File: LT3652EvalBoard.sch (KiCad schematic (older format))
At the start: 40 parts, among them U1 LT3652

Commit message: Upload of Rev 0.5
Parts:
- removed Pload2: USB_A, ms_connectors:WURTH_ELEKTRONIK_629104151021, symbol USB_A
- added Wvin1: TEST_1P, ms_pcb_test_points:HARWIN_S1751-46, symbol TEST_1P
- Pbat1, Pload1: footprint w_conn_jst-ph:b2b-ph-kl -> w_conn_jst-ph:s2b-ph-kl
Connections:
- net at Dvin1.3 (A), Pslr1.1 (P1), Pslr2.1 (P1)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: now also Wvin1.1
- no-connect marks 4 -> 1
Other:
- moved on the sheet: Cbat1, Pload1
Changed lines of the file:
@@
 LIBS:valves
 LIBS:w_analog
+LIBS:ESP8266
 LIBS:LT3652EvalBoard-cache
 EELAYER 25 0
@@
 F 0 "Pbat1" H 7905 4160 50  0000 C CNN
 F 1 "JST PH" V 8005 4010 50  0000 C CNN
-F 2 "w_conn_jst-ph:b2b-ph-kl" H 7905 4010 50  0001 C CNN
+F 2 "w_conn_jst-ph:s2b-ph-kl" H 7905 4010 50  0001 C CNN
 F 3 "" H 7905 4010 50  0000 C CNN
 	1    7905 4010
@@
 L CONN_01X02 Pload1
 U 1 1 56CF675B
-P 8880 3200
-F 0 "Pload1" H 8880 3350 50  0000 C CNN
-F 1 "JST PH" V 8980 3200 50  0000 C CNN
-F 2 "w_conn_jst-ph:b2b-ph-kl" H 8880 3200 50  0001 C CNN
-F 3 "" H 8880 3200 50  0000 C CNN
-	1    8880 3200
-	1    0    0    -1
-$EndComp
-Wire Wire Line
-	8080 3150 8680 3150
+P 8790 2975
+F 0 "Pload1" H 8790 3125 50  0000 C CNN
+F 1 "JST PH" V 8890 2975 50  0000 C CNN
+F 2 "w_conn_jst-ph:s2b-ph-kl" H 8790 2975 50  0001 C CNN
+F 3 "" H 8790 2975 50  0000 C CNN
+	1    8790 2975
+	1    0    0    -1
+$EndComp
 $Comp
 L GND #PWR011
 U 1 1 56CF694F
-P 8630 3400
-F 0 "#PWR011" H 8630 3150 50  0001 C CNN
-F 1 "GND" H 8630 3250 50  0000 C CNN
-F 2 "" H 8630 3400 50  0000 C CNN
-F 3 "" H 8630 3400 50  0000 C CNN
-	1    8630 3400
-	1    0    0    -1
-$EndComp
-Wire Wire Line
-	8630 3250 8630 3400
-Wire Wire Line
-	8630 3250 8680 3250
+P 8540 3175
+F 0 "#PWR011" H 8540 2925 50  0001 C CNN
+F 1 "GND" H 8540 3025 50  0000 C CNN
+F 2 "" H 8540 3175 50  0000 C CNN
+F 3 "" H 8540 3175 50  0000 C CNN
+	1    8540 3175
+	1    0    0    -1
+$EndComp
+Wire Wire Line
+	8540 3025 8540 3175
+Wire Wire Line
+	8540 3025 8590 3025
 Text Notes 6450 3800 0    39   ~ 0
 4.2V FLT
@@
 L CP1_Small Cbat1
 U 1 1 56D1522A
-P 8370 3270
-F 0 "Cbat1" H 8380 3340 50  0000 L CNN
-F 1 "100uF" H 8380 3190 50  0000 L CNN
-F 2 "Capacitors_ThroughHole:C_Radial_D5_L6_P2.5" H 8370 3270 50  0001 C CNN
-F 3 "" H 8370 3270 50  0000 C CNN
-	1    8370 3270
-	1    0    0    -1
-$EndComp
-Wire Wire Line
-	8370 3370 8370 3385
-Wire Wire Line
-	8370 3385 8630 3385
-Connection ~ 8630 3385
-$Comp
-L USB_A Pload2
-U 1 1 56D16751
-P 8915 2640
-F 0 "Pload2" H 9115 2440 50  0000 C CNN
-F 1 "USB_A" H 8865 2840 50  0000 C CNN
-F 2 "ms_connectors:WURTH_ELEKTRONIK_629104151021" V 8865 2540 50  0001 C CNN
-F 3 "" V 8865 2540 50  0000 C CNN
-	1    8915 2640
-	0    1    1    0
-$EndComp
-$Comp
-L GND #PWR012
-U 1 1 56D16B0E
-P 8555 2865
-F 0 "#PWR012" H 8555 2615 50  0001 C CNN
-F 1 "GND" H 8555 2715 50  0000 C CNN
-F 2 "" H 8555 2865 50  0000 C CNN
-F 3 "" H 8555 2865 50  0000 C CNN
-	1    8555 2865
-	1    0    0    -1
-$EndComp
-Wire Wire Line
-	8555 2865 8555 2740
-Wire Wire Line
-	8555 2740 8615 2740
-NoConn ~ 8615 2540
-NoConn ~ 8615 2640
-NoConn ~ 9015 2940
-Wire Wire Line
-	8370 3170 8370 3150
-Connection ~ 8370 3150
-Wire Wire Line
-	8080 2440 8615 2440
+P 8280 3045
+F 0 "Cbat1" H 8290 3115 50  0000 L CNN
+F 1 "100uF" H 8290 2965 50  0000 L CNN
+F 2 "Capacitors_ThroughHole:C_Radial_D5_L6_P2.5" H 8280 3045 50  0001 C CNN
+F 3 "" H 8280 3045 50  0000 C CNN
+	1    8280 3045
+	1    0    0    -1
+$EndComp
+Wire Wire Line
+	8280 3145 8280 3160
+Wire Wire Line
+	8280 3160 8540 3160
+Connection ~ 8540 3160
+Wire Wire Line
+	8280 2850 8280 2945
+Connection ~ 8280 2925
 $Comp
 L CONN_01X02 Pslr1
@@
 $EndComp
 Wire Wire Line
-	7980 2925 8080 2925
-Connection ~ 8080 2925
-Wire Wire Line
 	7360 3175 7360 3960
 Wire Wire Line
@@
 Connection ~ 7625 2675
 $Comp
-L PWR_FLAG #FLG013
+L PWR_FLAG #FLG012
 U 1 1 56D7B958
-P 8315 2400
-F 0 "#FLG013" H 8315 2495 50  0001 C CNN
-F 1 "PWR_FLAG" H 8315 2580 50  0000 C CNN
-F 2 "" H 8315 2400 50  0000 C CNN
-F 3 "" H 8315 2400 50  0000 C CNN
-	1    8315 2400
-	1    0    0    -1
-$EndComp
-Wire Wire Line
-	8315 2400 8315 2440
-Connection ~ 8315 2440
+P 8280 2850
+F 0 "#FLG012" H 8280 2945 50  0001 C CNN
+F 1 "PWR_FLAG" H 8280 3030 50  0000 C CNN
+F 2 "" H 8280 2850 50  0000 C CNN
+F 3 "" H 8280 2850 50  0000 C CNN
+	1    8280 2850
+	1    0    0    -1
+$EndComp
 $Comp
 L CONN_01X02 Pslr2
@@
 	3950 3805 3915 3805
 Wire Wire Line
-	8080 2440 8080 3150
-Wire Wire Line
 	7360 3960 7705 3960
+Wire Wire Line
+	8590 2925 7980 2925
+$Comp
+L TEST_1P Wvin1
+U 1 1 56F07523
+P 4670 1810
+F 0 "Wvin1" H 4670 2005 50  0000 C CNN
+F 1 "TEST_1P" H 4670 2010 50  0001 C CNN
+F 2 "ms_pcb_test_points:HARWIN_S1751-46" H 4870 1810 50  0001 C CNN
+F 3 "" H 4870 1810 50  0000 C CNN
+	1    4670 1810
+	1    0    0    -1
+$EndComp
+Wire Wire Line
+	4670 1810 4670 2190
+Connection ~ 4670 2190
 $EndSCHEMATC

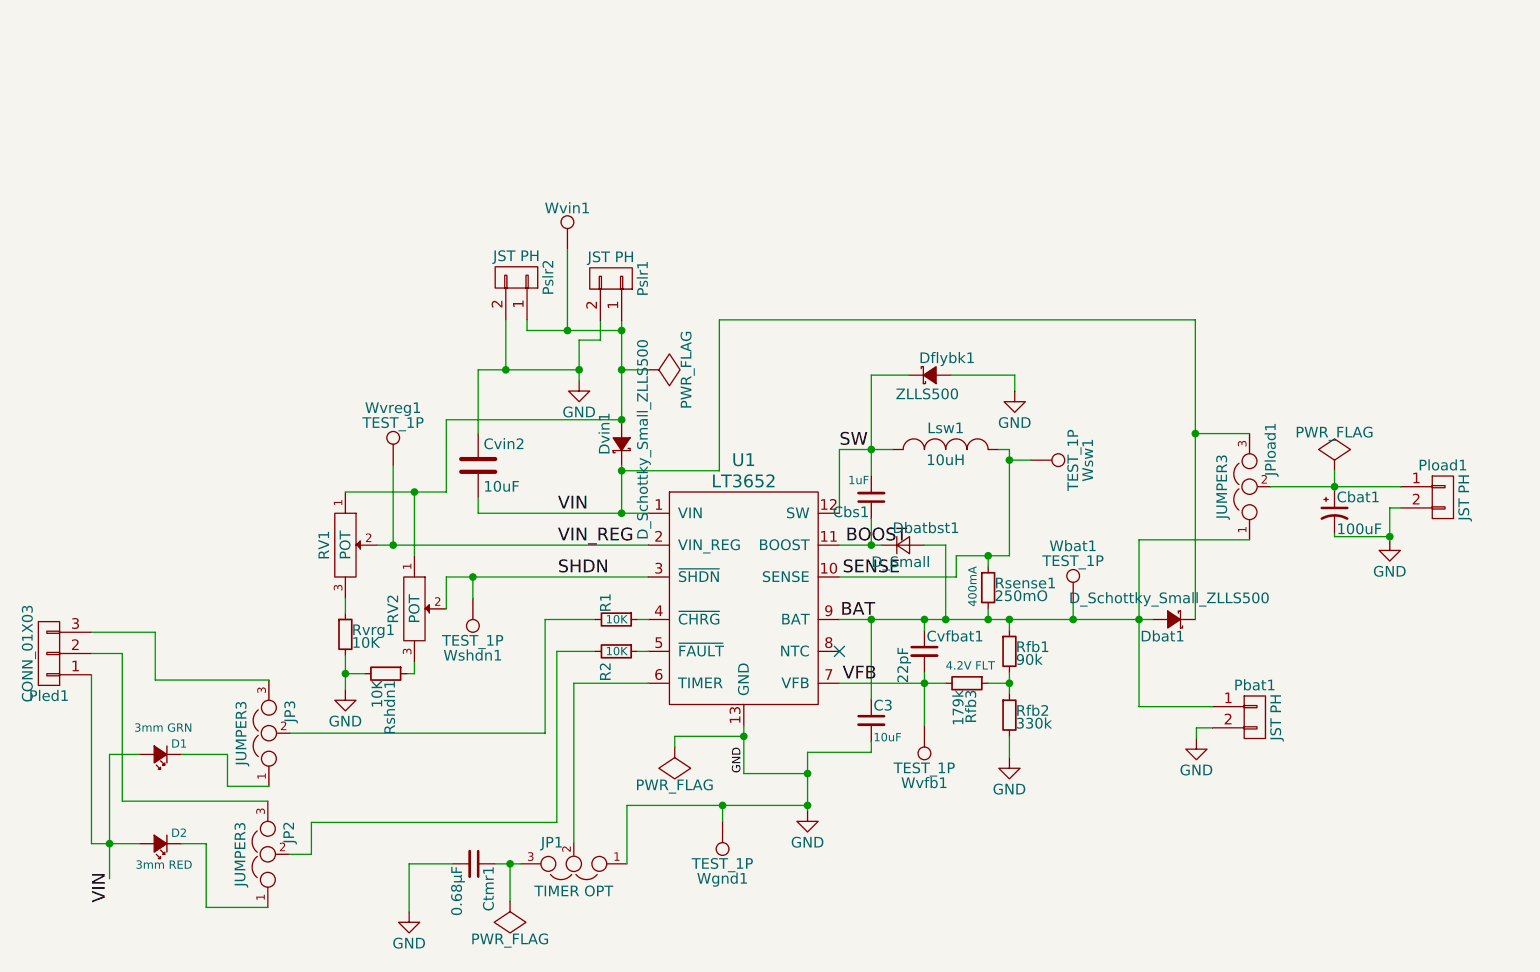
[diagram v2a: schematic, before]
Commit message: Rev 0.6 - Adds ability to add solar panel in series, plus separate blocking diode for parallel solar panel
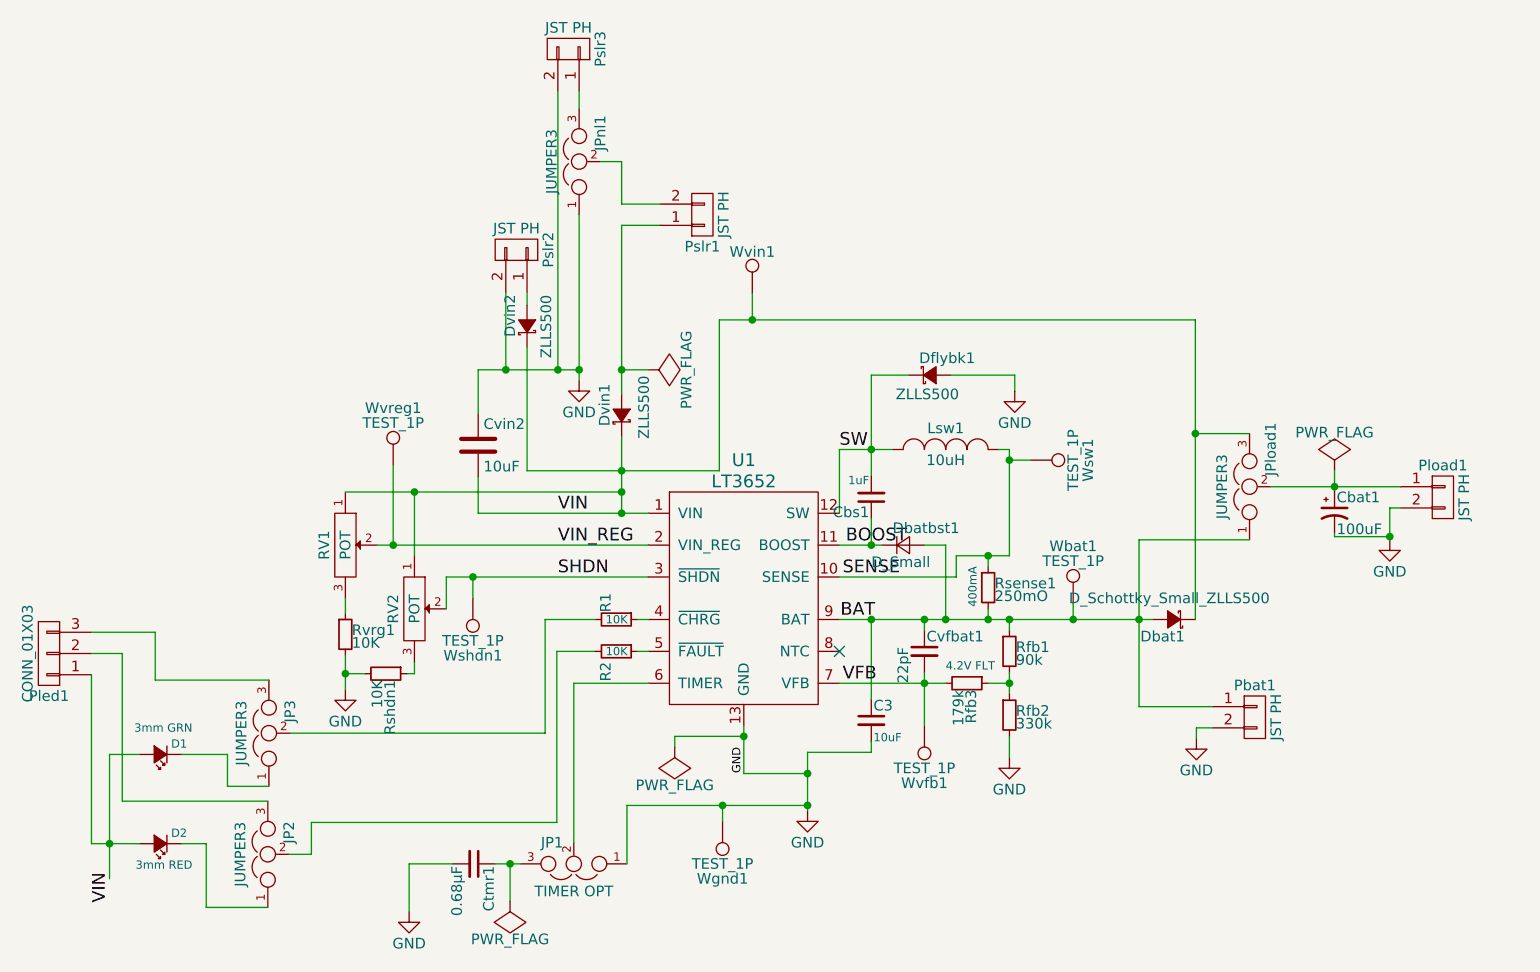
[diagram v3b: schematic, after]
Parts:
- added Dvin2: ZLLS500, ms_diodes:DIODES_INC_ZLLS500, symbol D_Schottky_Small_ZLLS500
- added JPnl1: JUMPER3, Pin_Headers:Pin_Header_Straight_1x03, symbol JUMPER3
- added Pslr1: JST PH, w_conn_jst-ph:b2b-ph-kl, symbol CONN_01X02
- Dvin1: value D_Schottky_Small_ZLLS500 -> ZLLS500
- renumbered Pslr1 to Pslr3
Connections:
- net GND: now also JPnl1.1
- net VIN: now also RV1.1, RV2.1, Wvin1.1, Dvin2.1 (K)
- new net: Dvin1.3 (A), Pslr1.1 (P1)
- new net: JPnl1.3, Pslr3.1 (P1)
- new net: Dvin2.3 (A), Pslr2.1 (P1)
- new net: JPnl1.2, Pslr1.2 (P2)
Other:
- moved on the sheet: Cvin2, Dvin1, Pslr2, Pslr3, Wvin1

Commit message: Fixed wrong footprint for Rsense1
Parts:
- Rsense1: footprint Capacitors_SMD:C_0805_HandSoldering -> Resistors_SMD:R_0805_HandSoldering
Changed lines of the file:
@@
 F 0 "Rsense1" H 6680 3420 50  0000 L CNN
 F 1 "250mO" H 6680 3360 50  0000 L CNN
-F 2 "Capacitors_SMD:C_0805_HandSoldering" H 6650 3400 50  0001 C CNN
+F 2 "Resistors_SMD:R_0805_HandSoldering" H 6650 3400 50  0001 C CNN
 F 3 "" H 6650 3400 50  0000 C CNN
 	1    6650 3400

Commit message: Rev 0.9
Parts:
- added Wsw0: TEST_1P, ms_pcb_test_points:HARWIN_S1751-46, symbol TEST_1P
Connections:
- net BAT: now also Pbat1.2 (P2); no longer Pbat1.1 (P1)
- net GND: now also Pbat1.1 (P1), Pload1.1 (P1), Pslr2.1 (P1), Pslr3.1 (P1); no longer Pbat1.2 (P2), Pload1.2 (P2), Pslr2.2 (P2), Pslr3.2 (P2)
- net SW: now also Wsw0.1
- net at Cbat1.1, JPload1.2: now also Pload1.2 (P2); no longer Pload1.1 (P1)
- net at Dvin1.3 (A): now also Pslr1.2 (P2); no longer Pslr1.1 (P1)
- net at JPnl1.3: now also Pslr3.2 (P2); no longer Pslr3.1 (P1)
- net at Dvin2.3 (A): now also Pslr2.2 (P2); no longer Pslr2.1 (P1)
- net at JPnl1.2: now also Pslr1.1 (P1); no longer Pslr1.2 (P2)
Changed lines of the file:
@@
 F 3 "" H 7905 4010 50  0000 C CNN
 	1    7905 4010
-	1    0    0    -1
+	1    0    0    1
 $EndComp
 $Comp
@@
 F 3 "" H 8790 2975 50  0000 C CNN
 	1    8790 2975
-	1    0    0    -1
+	1    0    0    1
 $EndComp
 $Comp
@@
 F 3 "" H 4675 865 50  0000 C CNN
 	1    4675 865
-	0    1    -1   0
+	0    -1   -1   0
 $EndComp
 $Comp
@@
 F 3 "" H 4430 1810 50  0000 C CNN
 	1    4430 1810
-	0    1    -1   0
+	0    -1   -1   0
 $EndComp
 Text Label 2515 4740 3    60   ~ 0
@@
 	7630 4060 7705 4060
 Wire Wire Line
-	5950 3050 5950 2750
+	5950 2655 5950 3050
 Wire Wire Line
 	6100 2400 6100 2875
@@
 F 3 "" H 5305 1645 50  0000 C CNN
 	1    5305 1645
-	1    0    0    1
+	1    0    0    -1
 $EndComp
 Wire Wire Line
@@
 	4625 1065 4625 2375
 Connection ~ 4625 2375
+$Comp
+L TEST_1P Wsw0
+U 1 1 57057E28
+P 5950 2655
+F 0 "Wsw0" H 5950 2850 50  0000 C CNN
+F 1 "TEST_1P" H 5950 2855 50  0001 C CNN
+F 2 "ms_pcb_test_points:HARWIN_S1751-46" H 6150 2655 50  0001 C CNN
+F 3 "" H 6150 2655 50  0000 C CNN
+	1    5950 2655
+	1    0    0    -1
+$EndComp
+Connection ~ 5950 2750
 $EndSCHEMATC

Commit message: Rev 0.10
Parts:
- removed Dvin2: ZLLS500, ms_diodes:DIODES_INC_ZLLS500, symbol D_Schottky_Small_ZLLS500
- removed JPnl1: JUMPER3, Pin_Headers:Pin_Header_Straight_1x03, symbol JUMPER3
- removed Pslr3: JST PH, w_conn_jst-ph:b2b-ph-kl, symbol CONN_01X02
- added JP4: Jumper_NO_Small, Resistors_SMD:R_0805_HandSoldering, symbol Jumper_NO_Small
- added JP5: Jumper_NC_Small, Resistors_SMD:R_0805_HandSoldering, symbol Jumper_NC_Small
- added Wbst1: TEST_1P, Measurement_Points:Measurement_Point_Round-SMD-Pad_Small, symbol TEST_1P
- RV1, RV2: symbol POT -> POT-RESCUE-LT3652EvalBoard
- Wsw2: renamed from Wsw0; footprint ms_pcb_test_points:HARWIN_S1751-46 -> Measurement_Points:Measurement_Point_Round-SMD-Pad_Small
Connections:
- net BOOST: now also Wbst1.1
- net GND: now also JP5.1
- net at Pslr2.2 (P2): now also JP4.2
- net at Pslr1.1 (P1): now also JP4.1, JP5.2
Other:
- moved on the sheet: Pslr1, Pslr2
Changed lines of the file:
@@
 EESchema Schematic File Version 2
+LIBS:LT3652EvalBoard-rescue
 LIBS:power
 LIBS:device
@@
 Sheet 1 1
 Title "LT3652 Evaluation Board"
-Date "2016-03-15"
-Rev "0.3"
+Date "2017-02-27"
+Rev "0.4"
 Comp "Malcolm Spiteri"
 Comment1 ""
@@
 L GND #PWR03
 U 1 1 56C2981A
-P 4725 2425
-F 0 "#PWR03" H 4725 2175 50  0001 C CNN
-F 1 "GND" H 4725 2275 50  0000 C CNN
-F 2 "" H 4725 2425 50  0000 C CNN
-F 3 "" H 4725 2425 50  0000 C CNN
-	1    4725 2425
+P 4675 2430
+F 0 "#PWR03" H 4675 2180 50  0001 C CNN
+F 1 "GND" H 4675 2280 50  0000 C CNN
+F 2 "" H 4675 2430 50  0000 C CNN
+F 3 "" H 4675 2430 50  0000 C CNN
+	1    4675 2430
 	1    0    0    -1
 $EndComp
@@
 $EndComp
 $Comp
-L POT RV1
+L POT-RESCUE-LT3652EvalBoard RV1
 U 1 1 56C645D0
 P 3625 3200
@@
 $EndComp
 $Comp
-L POT RV2
+L POT-RESCUE-LT3652EvalBoard RV2
 U 1 1 56C6527D
 P 3950 3500
@@
 U 1 1 56D0804A
 P 6650 3400
-F 0 "Rsense1" H 6680 3420 50  0000 L CNN
-F 1 "250mO" H 6680 3360 50  0000 L CNN
+F 0 "Rsense1" V 6715 3260 43  0000 L CNN
+F 1 "250mO" V 6785 3265 43  0000 L CNN
 F 2 "Resistors_SMD:R_0805_HandSoldering" H 6650 3400 50  0001 C CNN
 F 3 "" H 6650 3400 50  0000 C CNN
@@
 $EndComp
 $Comp
-L CONN_01X02 Pslr3
-U 1 1 56D5EAF0
-P 4675 865
-F 0 "Pslr3" H 4675 1015 50  0000 C CNN
-F 1 "JST PH" V 4775 865 50  0000 C CNN
-F 2 "w_conn_jst-ph:b2b-ph-kl" H 4675 865 50  0001 C CNN
-F 3 "" H 4675 865 50  0000 C CNN
-	1    4675 865
-	0    -1   -1   0
-$EndComp
-$Comp
 L D_Schottky_Small_ZLLS500 Dbat1
 U 1 1 56D71C0A
@@
 L CONN_01X02 Pslr2
 U 1 1 56D8B1A1
-P 4430 1810
-F 0 "Pslr2" H 4430 1960 50  0000 C CNN
-F 1 "JST PH" V 4530 1810 50  0000 C CNN
-F 2 "w_conn_jst-ph:b2b-ph-kl" H 4430 1810 50  0001 C CNN
-F 3 "" H 4430 1810 50  0000 C CNN
-	1    4430 1810
+P 4430 1485
+F 0 "Pslr2" H 4430 1635 50  0000 C CNN
+F 1 "JST PH" V 4530 1485 50  0000 C CNN
+F 2 "w_conn_jst-ph:b2b-ph-kl" H 4430 1485 50  0001 C CNN
+F 3 "" H 4430 1485 50  0000 C CNN
+	1    4430 1485
 	0    -1   -1   0
 $EndComp
@@
 $EndComp
 $Comp
-L D_Schottky_Small_ZLLS500 Dvin2
-U 1 1 56F3429B
-P 4480 2170
-F 0 "Dvin2" H 4430 2250 50  0000 L CNN
-F 1 "ZLLS500" H 4330 2080 50  0000 L CNN
-F 2 "ms_diodes:DIODES_INC_ZLLS500" V 4480 2170 50  0001 C CNN
-F 3 "" V 4480 2170 50  0000 C CNN
-	1    4480 2170
+L CONN_01X02 Pslr1
+U 1 1 56F3F4BC
+P 4875 1480
+F 0 "Pslr1" H 4875 1630 50  0000 C CNN
+F 1 "JST PH" V 4975 1480 50  0000 C CNN
+F 2 "w_conn_jst-ph:b2b-ph-kl" H 4875 1480 50  0001 C CNN
+F 3 "" H 4875 1480 50  0000 C CNN
+	1    4875 1480
 	0    -1   -1   0
 $EndComp
+$Comp
+L TEST_1P Wsw2
+U 1 1 57057E28
+P 5950 2655
+F 0 "Wsw2" H 5950 2925 50  0000 C CNN
+F 1 "TEST_1P" H 5950 2855 50  0000 C CNN
+F 2 "Measurement_Points:Measurement_Point_Round-SMD-Pad_Small" H 6150 2655 50  0001 C CNN
+F 3 "" H 6150 2655 50  0000 C CNN
+	1    5950 2655
+	1    0    0    -1
+$EndComp
+$Comp
+L Jumper_NO_Small JP4
+U 1 1 58B30013
+P 4645 1970
+F 0 "JP4" H 4645 2050 50  0000 C CNN
+F 1 "Jumper_NO_Small" H 4655 1910 50  0001 C CNN
+F 2 "Resistors_SMD:R_0805_HandSoldering" H 4645 1970 50  0001 C CNN
+F 3 "" H 4645 1970 50  0000 C CNN
+	1    4645 1970
+	-1   0    0    1
+$EndComp
 Wire Wire Line
 	5800 4175 5800 4450
@@
 	4250 2880 4250 3050
 Wire Wire Line
-	4725 1645 4725 2425
-Wire Wire Line
 	4250 2580 4250 2375
-Wire Wire Line
-	4250 2375 4725 2375
-Connection ~ 4725 2375
 Connection ~ 4925 3050
-Wire Wire Line
-	4925 2375 5050 2375
-Connection ~ 4925 2375
 Wire Wire Line
 	5175 4150 5175 4100
@@
 	4250 3050 5050 3050
 Wire Wire Line
-	4925 1695 4925 2490
-Wire Wire Line
 	8280 3145 8280 3160
 Wire Wire Line
@@
 	6100 3925 6100 3550
 Wire Wire Line
-	4480 2850 5385 2850
-Wire Wire Line
 	5385 2850 5385 2140
 Connection ~ 4925 2850
@@
 Connection ~ 7625 2675
 Wire Wire Line
-	4380 2010 4380 2375
+	4380 1685 4380 2375
 Connection ~ 4380 2375
 Wire Wire Line
@@
 	5540 2015 5540 2140
 Connection ~ 5540 2140
-Wire Wire Line
-	4480 2270 4480 2850
 Connection ~ 4925 2950
-Wire Wire Line
-	4480 2010 4480 2070
-$Comp
-L JUMPER3 JPnl1
-U 1 1 56F3EE86
-P 4725 1395
-F 0 "JPnl1" H 4775 1295 50  0000 L CNN
-F 1 "JUMPER3" H 4725 1495 50  0000 C BNN
-F 2 "Pin_Headers:Pin_Header_Straight_1x03" H 4725 1395 50  0001 C CNN
-F 3 "" H 4725 1395 50  0000 C CNN
-	1    4725 1395
+Connection ~ 5950 2750
+Wire Wire Line
+	4925 1680 4925 2490
+Wire Wire Line
+	4250 2375 4825 2375
+Wire Wire Line
+	4675 2375 4675 2430
+Wire Wire Line
+	5050 2375 4925 2375
+Connection ~ 4925 2375
+Connection ~ 4675 2375
+Wire Wire Line
+	5385 2850 4925 2850
+Wire Wire Line
+	4545 1970 4480 1970
+Wire Wire Line
+	4480 1970 4480 1685
+Wire Wire Line
+	4745 1970 4825 1970
+Wire Wire Line
+	4825 1680 4825 2015
+$Comp
+L Jumper_NC_Small JP5
+U 1 1 58B31A07
+P 4825 2115
+F 0 "JP5" H 4825 2195 50  0000 C CNN
+F 1 "Jumper_NC_Small" H 4835 2055 50  0001 C CNN
+F 2 "Resistors_SMD:R_0805_HandSoldering" H 4825 2115 50  0001 C CNN
+F 3 "" H 4825 2115 50  0000 C CNN
+	1    4825 2115
 	0    -1   -1   0
 $EndComp
-$Comp
-L CONN_01X02 Pslr1
-U 1 1 56F3F4BC
-P 5305 1645
-F 0 "Pslr1" H 5305 1795 50  0000 C CNN
-F 1 "JST PH" V 5405 1645 50  0000 C CNN
-F 2 "w_conn_jst-ph:b2b-ph-kl" H 5305 1645 50  0001 C CNN
-F 3 "" H 5305 1645 50  0000 C CNN
-	1    5305 1645
-	1    0    0    -1
-$EndComp
-Wire Wire Line
-	5105 1695 4925 1695
-Wire Wire Line
-	4825 1395 4925 1395
-Wire Wire Line
-	4925 1395 4925 1595
-Wire Wire Line
-	4925 1595 5105 1595
-Wire Wire Line
-	4725 1065 4725 1145
-Wire Wire Line
-	4625 1065 4625 2375
-Connection ~ 4625 2375
-$Comp
-L TEST_1P Wsw0
-U 1 1 57057E28
-P 5950 2655
-F 0 "Wsw0" H 5950 2850 50  0000 C CNN
-F 1 "TEST_1P" H 5950 2855 50  0001 C CNN
-F 2 "ms_pcb_test_points:HARWIN_S1751-46" H 6150 2655 50  0001 C CNN
-F 3 "" H 6150 2655 50  0000 C CNN
-	1    5950 2655
-	1    0    0    -1
-$EndComp
-Connection ~ 5950 2750
+Connection ~ 4825 1970
+Wire Wire Line
+	4825 2375 4825 2215
+$Comp
+L TEST_1P Wbst1
+U 1 1 58B53853
+P 6410 3035
+F 0 "Wbst1" H 6410 3305 50  0000 C CNN
+F 1 "TEST_1P" H 6410 3235 50  0000 C CNN
+F 2 "Measurement_Points:Measurement_Point_Round-SMD-Pad_Small" H 6610 3035 50  0001 C CNN
+F 3 "" H 6610 3035 50  0000 C CNN
+	1    6410 3035
+	0    1    1    0
+$EndComp
+Wire Wire Line
+	6410 3035 6135 3035
+Wire Wire Line
+	6135 3035 6135 3100
+Wire Wire Line
+	6135 3100 6100 3100
+Connection ~ 6100 3100
 $EndSCHEMATC
